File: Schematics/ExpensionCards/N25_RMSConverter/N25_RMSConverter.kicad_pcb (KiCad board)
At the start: 2 copper layers, 100.5 x 64.5 mm, 72 parts

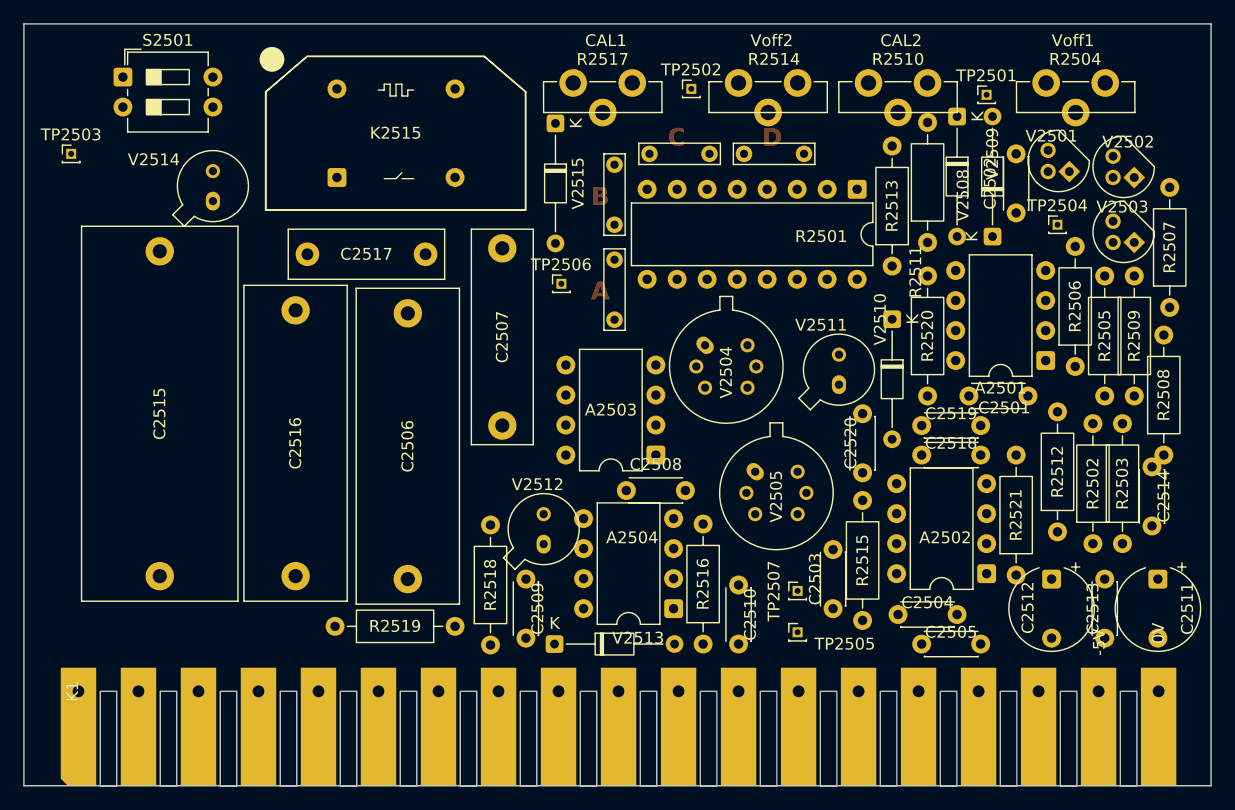
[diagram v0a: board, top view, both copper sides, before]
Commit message: Reworked N20/N21
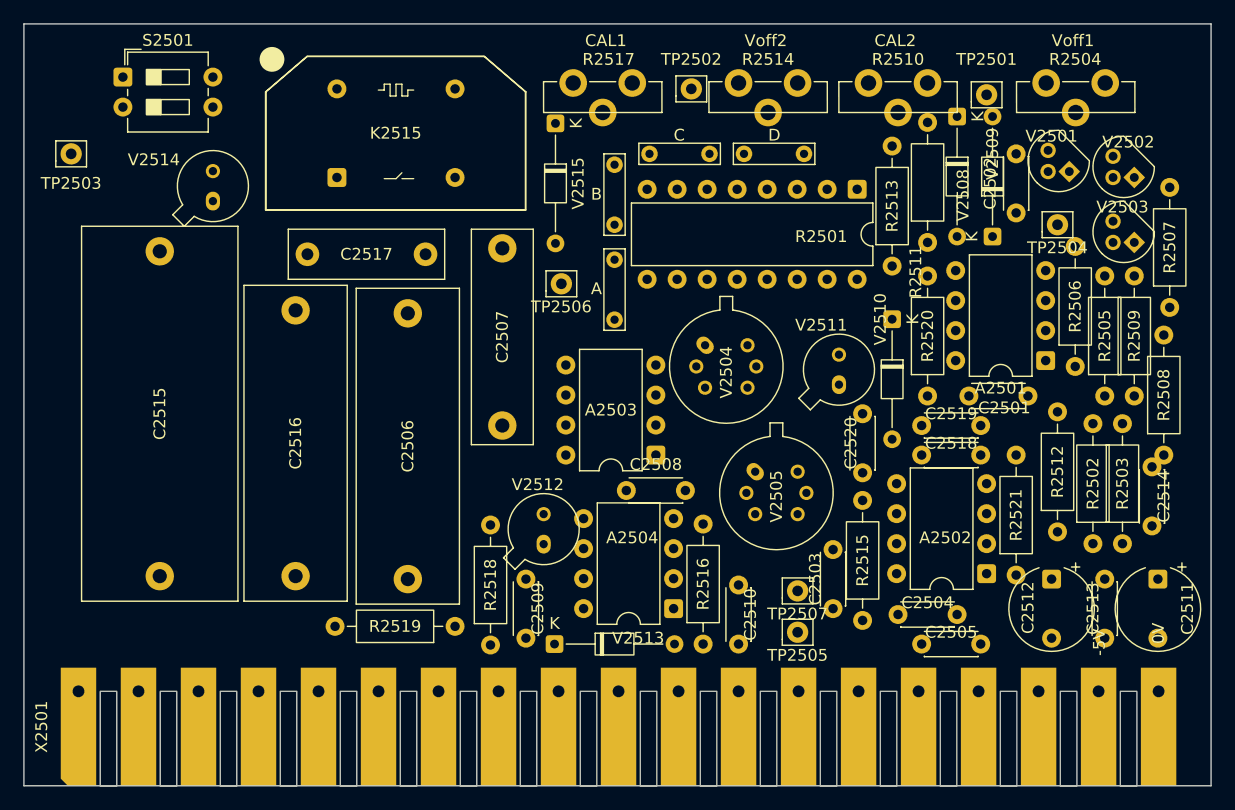
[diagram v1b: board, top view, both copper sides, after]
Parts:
- R2504, R2510, R2514, R2517: footprint PM2528:Potentiometer horizontal ceramic -> PM2528:Trimmer vertical
- TP2501, TP2502, TP2503, TP2504, TP2505, TP2506, TP2507: footprint Connector_PinHeader_1.00mm:PinHeader_1x01_P1.00mm_Vertical -> Connector_Pin:Pin_D0.9mm_L10.0mm_W2.4mm_FlatFork
- renumbered JP4 to JP2501, JP3 to JP2502, JP2 to JP2503, JP1 to JP2504, K1 to X2501
